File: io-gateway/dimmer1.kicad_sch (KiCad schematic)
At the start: 30 parts

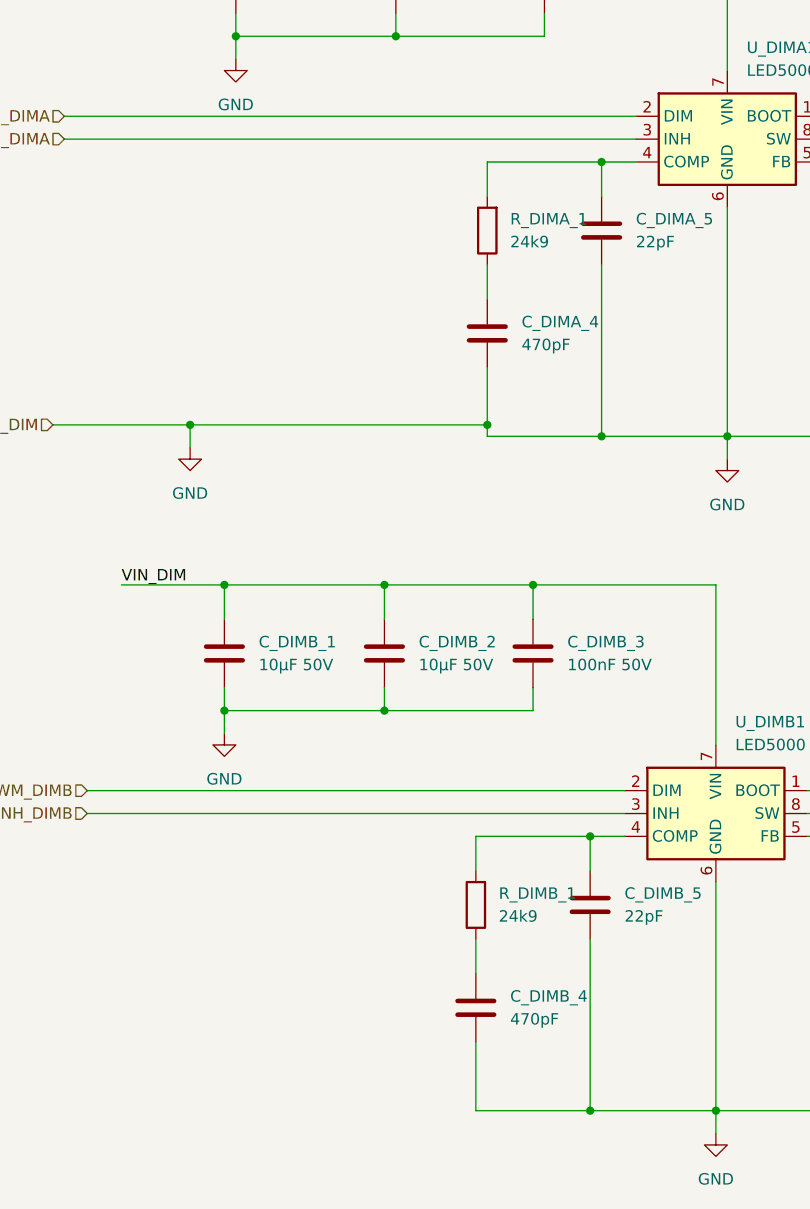
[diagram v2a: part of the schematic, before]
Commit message: add RS485
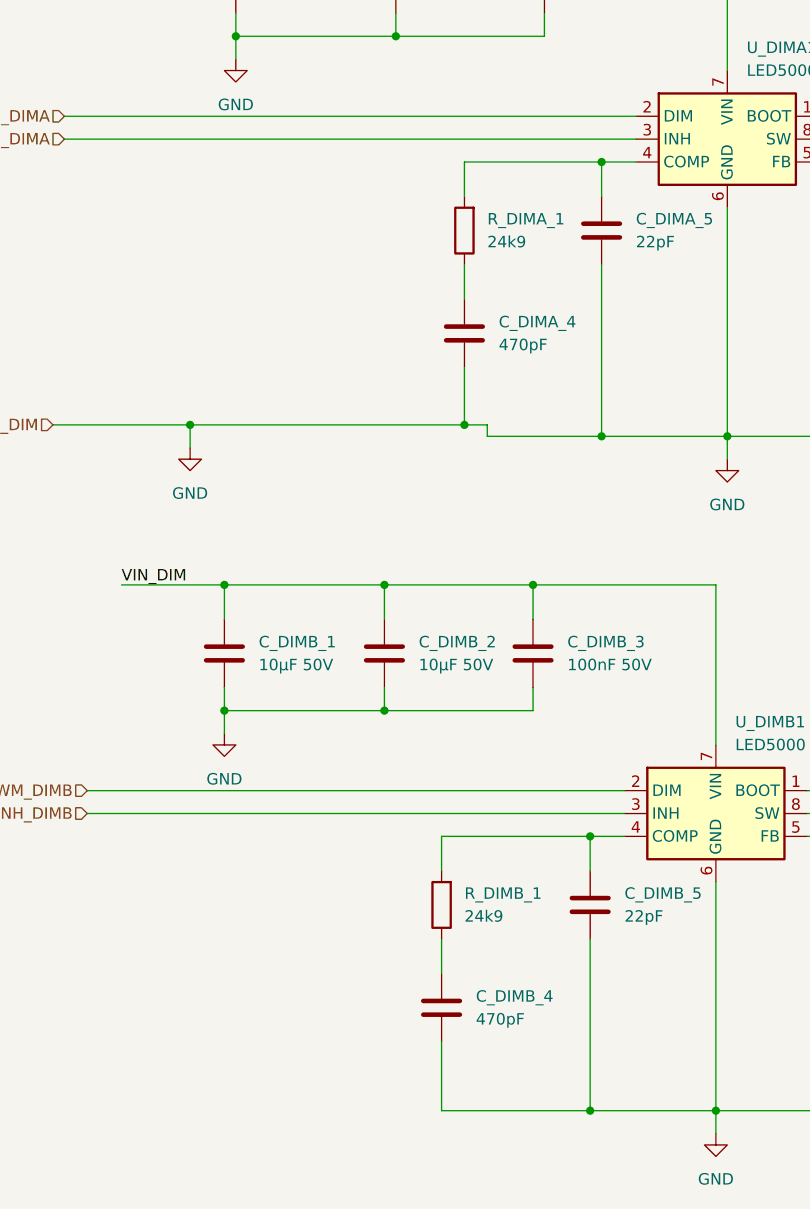
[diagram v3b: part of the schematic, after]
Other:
- moved on the sheet: C_DIMA_4, C_DIMB_4, R_DIMA_1, R_DIMB_1
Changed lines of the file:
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@@
 	)
 	(junction
-		(at 71.12 78.74)
-		(diameter 0)
-		(color 0 0 0 0)
-	)
-	(junction
 		(at 130.81 154.94)
 		(diameter 0)
@@
 	)
 	(junction
+		(at 68.58 78.74)
+		(diameter 0)
+		(color 0 0 0 0)
+	)
+	(junction
 		(at 83.82 49.53)
 		(diameter 0)
@@
 	(wire
 		(pts
-			(xy 71.12 72.39) (xy 71.12 78.74)
+			(xy 68.58 72.39) (xy 68.58 78.74)
 		)
 		(stroke
@@
 	(wire
 		(pts
-			(xy 82.55 154.94) (xy 69.85 154.94)
+			(xy 82.55 154.94) (xy 66.04 154.94)
 		)
 		(stroke
@@
 	(wire
 		(pts
-			(xy 82.55 124.46) (xy 69.85 124.46)
+			(xy 82.55 124.46) (xy 66.04 124.46)
 		)
 		(stroke
@@
 	(wire
 		(pts
+			(xy 68.58 78.74) (xy 71.12 78.74)
+		)
+		(stroke
+			(width 0)
+			(type default)
+		)
+	)
+	(wire
+		(pts
 			(xy 177.8 80.01) (xy 191.77 80.01)
 		)
@@
 	(wire
 		(pts
-			(xy 69.85 124.46) (xy 69.85 128.27)
+			(xy 66.04 124.46) (xy 66.04 128.27)
 		)
 		(stroke
@@
 	(wire
 		(pts
-			(xy 69.85 147.32) (xy 69.85 154.94)
+			(xy 66.04 147.32) (xy 66.04 154.94)
 		)
 		(stroke
@@
 	(wire
 		(pts
-			(xy 71.12 60.96) (xy 71.12 64.77)
+			(xy 68.58 60.96) (xy 68.58 64.77)
 		)
 		(stroke
@@
 	(wire
 		(pts
-			(xy 83.82 49.53) (xy 71.12 49.53)
+			(xy 83.82 49.53) (xy 68.58 49.53)
 		)
 		(stroke
@@
 	(wire
 		(pts
-			(xy 38.1 78.74) (xy 71.12 78.74)
+			(xy 38.1 78.74) (xy 68.58 78.74)
 		)
 		(stroke
@@
 	(wire
 		(pts
-			(xy 71.12 49.53) (xy 71.12 53.34)
+			(xy 68.58 49.53) (xy 68.58 53.34)
 		)
 		(stroke
@@
 	(wire
 		(pts
-			(xy 69.85 135.89) (xy 69.85 139.7)
+			(xy 66.04 135.89) (xy 66.04 139.7)
 		)
 		(stroke
@@
 	(symbol
 		(lib_id "Device:R")
-		(at 71.12 57.15 180)
+		(at 68.58 57.15 180)
 		(unit 1)
 		(exclude_from_sim no)
@@
 		(fields_autoplaced yes)
 		(property "Reference" "R_DIMA_1"
-			(at 73.66 55.8799 0)
+			(at 71.12 55.8799 0)
 			(effects
 				(font
@@
 		)
 		(property "Value" "24k9"
-			(at 73.66 58.4199 0)
+			(at 71.12 58.4199 0)
 			(effects
 				(font
@@
 		)
 		(property "Footprint" "Resistor_SMD:R_0603_1608Metric"
-			(at 72.898 57.15 90)
+			(at 70.358 57.15 90)
 			(effects
 				(font
@@
 		)
 		(property "Datasheet" "~"
-			(at 71.12 57.15 0)
+			(at 68.58 57.15 0)
 			(effects
 				(font
@@
 		)
 		(property "Description" "Resistor"
-			(at 71.12 57.15 0)
+			(at 68.58 57.15 0)
 			(effects
 				(font
@@
 	(symbol
 		(lib_id "Device:R")
-		(at 69.85 132.08 180)
+		(at 66.04 132.08 180)
 		(unit 1)
 		(exclude_from_sim no)
@@
 		(fields_autoplaced yes)
 		(property "Reference" "R_DIMB_1"
-			(at 72.39 130.8099 0)
+			(at 68.58 130.8099 0)
 			(effects
 				(font
@@
 		)
 		(property "Value" "24k9"
-			(at 72.39 133.3499 0)
+			(at 68.58 133.3499 0)
 			(effects
 				(font
@@
 		)
 		(property "Footprint" "Resistor_SMD:R_0603_1608Metric"
-			(at 71.628 132.08 90)
+			(at 67.818 132.08 90)
 			(effects
 				(font
@@
 		)
 		(property "Datasheet" "~"
-			(at 69.85 132.08 0)
+			(at 66.04 132.08 0)
 			(effects
 				(font
@@
 		)
 		(property "Description" "Resistor"
-			(at 69.85 132.08 0)
+			(at 66.04 132.08 0)
 			(effects
 				(font
@@
 	(symbol
 		(lib_id "Device:C")
-		(at 71.12 68.58 0)
+		(at 68.58 68.58 0)
 		(unit 1)
 		(exclude_from_sim no)
@@
 		(fields_autoplaced yes)
 		(property "Reference" "C_DIMA_4"
-			(at 74.93 67.3099 0)
+			(at 72.39 67.3099 0)
 			(effects
 				(font
@@
 		)
 		(property "Value" "470pF"
-			(at 74.93 69.8499 0)
+			(at 72.39 69.8499 0)
 			(effects
 				(font
@@
 		)
 		(property "Footprint" "Capacitor_SMD:C_0603_1608Metric"
-			(at 72.0852 72.39 0)
+			(at 69.5452 72.39 0)
 			(effects
 				(font
@@
 		)
 		(property "Datasheet" "~"
-			(at 71.12 68.58 0)
+			(at 68.58 68.58 0)
 			(effects
 				(font
@@
 		)
 		(property "Description" "Unpolarized capacitor"
-			(at 71.12 68.58 0)
+			(at 68.58 68.58 0)
 			(effects
 				(font
@@
 	(symbol
 		(lib_id "Device:C")
-		(at 69.85 143.51 0)
+		(at 66.04 143.51 0)
 		(unit 1)
 		(exclude_from_sim no)
@@
 		(fields_autoplaced yes)
 		(property "Reference" "C_DIMB_4"
-			(at 73.66 142.2399 0)
+			(at 69.85 142.2399 0)
 			(effects
 				(font
@@
 		)
 		(property "Value" "470pF"
-			(at 73.66 144.7799 0)
+			(at 69.85 144.7799 0)
 			(effects
 				(font
@@
 		)
 		(property "Footprint" "Capacitor_SMD:C_0603_1608Metric"
-			(at 70.8152 147.32 0)
+			(at 67.0052 147.32 0)
 			(effects
 				(font
@@
 		)
 		(property "Datasheet" "~"
-			(at 69.85 143.51 0)
+			(at 66.04 143.51 0)
 			(effects
 				(font
@@
 		)
 		(property "Description" "Unpolarized capacitor"
-			(at 69.85 143.51 0)
+			(at 66.04 143.51 0)
 			(effects
 				(font

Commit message: fix minor issues
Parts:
- added RS_DIMA_2, RS_DIMB_2: R, Resistor_SMD:R_1206_3216Metric, symbol Device:R
- added R_DIMB_3, R_DIMB_4: 100k, Resistor_SMD:R_0603_1608Metric, symbol Device:R
- R_DIMA_1, R_DIMB_1: value 24k9 -> 33k
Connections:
- net DIM_VLED-_A: now also RS_DIMA_2.1
- net DIM_VLED-_B: now also RS_DIMB_2.1
- net GND: now also RS_DIMA_2.2, RS_DIMB_2.2
- net at C_DIMA_5.1, R_DIMA_1.2, U_DIMA1.4 (COMP): now also R_DIMB_3.2
- net at C_DIMA_4.1, R_DIMA_1.1: now also R_DIMB_3.1
- net at C_DIMB_5.1, R_DIMB_1.2, U_DIMB1.4 (COMP): now also R_DIMB_4.2
- net at C_DIMB_4.1, R_DIMB_1.1: now also R_DIMB_4.1
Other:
- moved on the sheet: C_DIMA_7, C_DIMA_8, C_DIMB_7, C_DIMB_8, RS_DIMA_1, RS_DIMB_1
